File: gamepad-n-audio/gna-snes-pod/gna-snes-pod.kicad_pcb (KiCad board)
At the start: 2 copper layers, 78 x 43 mm, 12 parts, among them J1 SNES, J2 SNES, J3 Gamepads, J4 SNES, J5 SNES

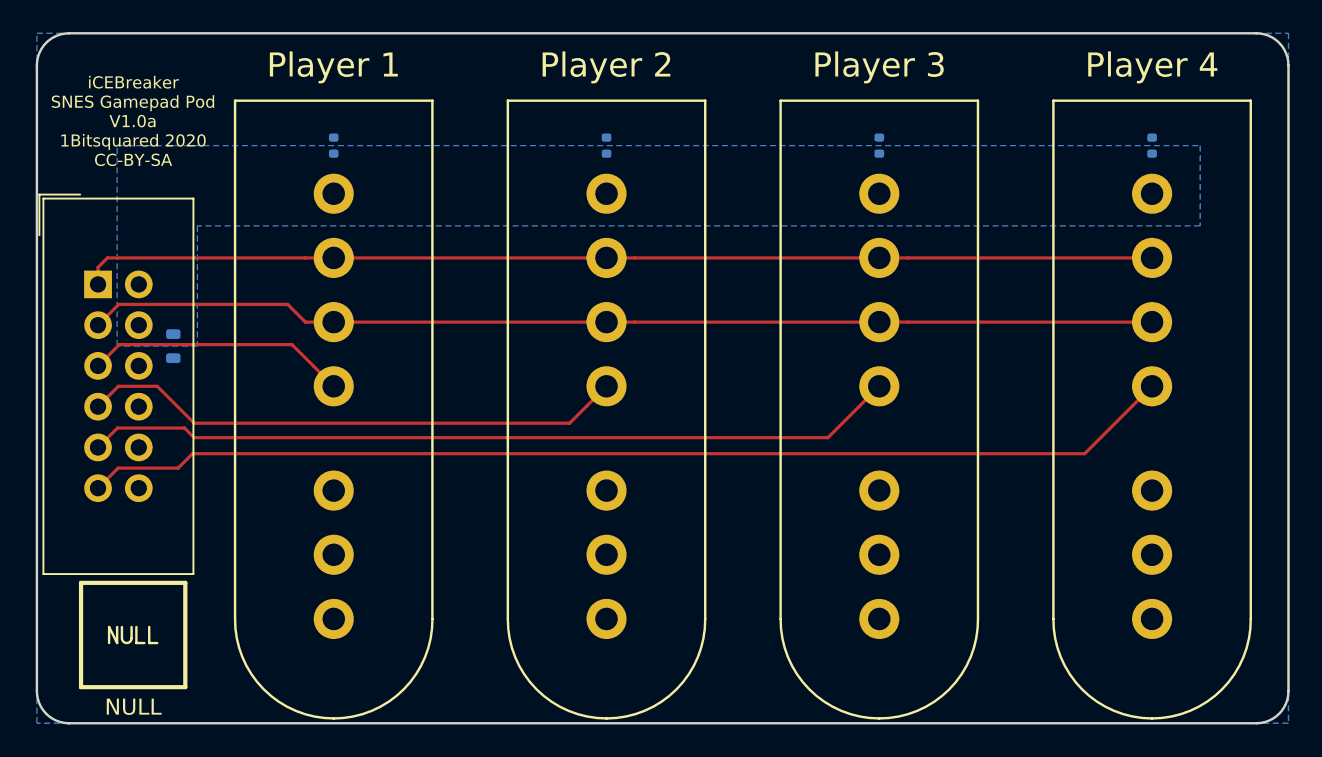
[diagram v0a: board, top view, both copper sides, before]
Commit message: gna SNES pod: Replaced back side ground fill with large traces.
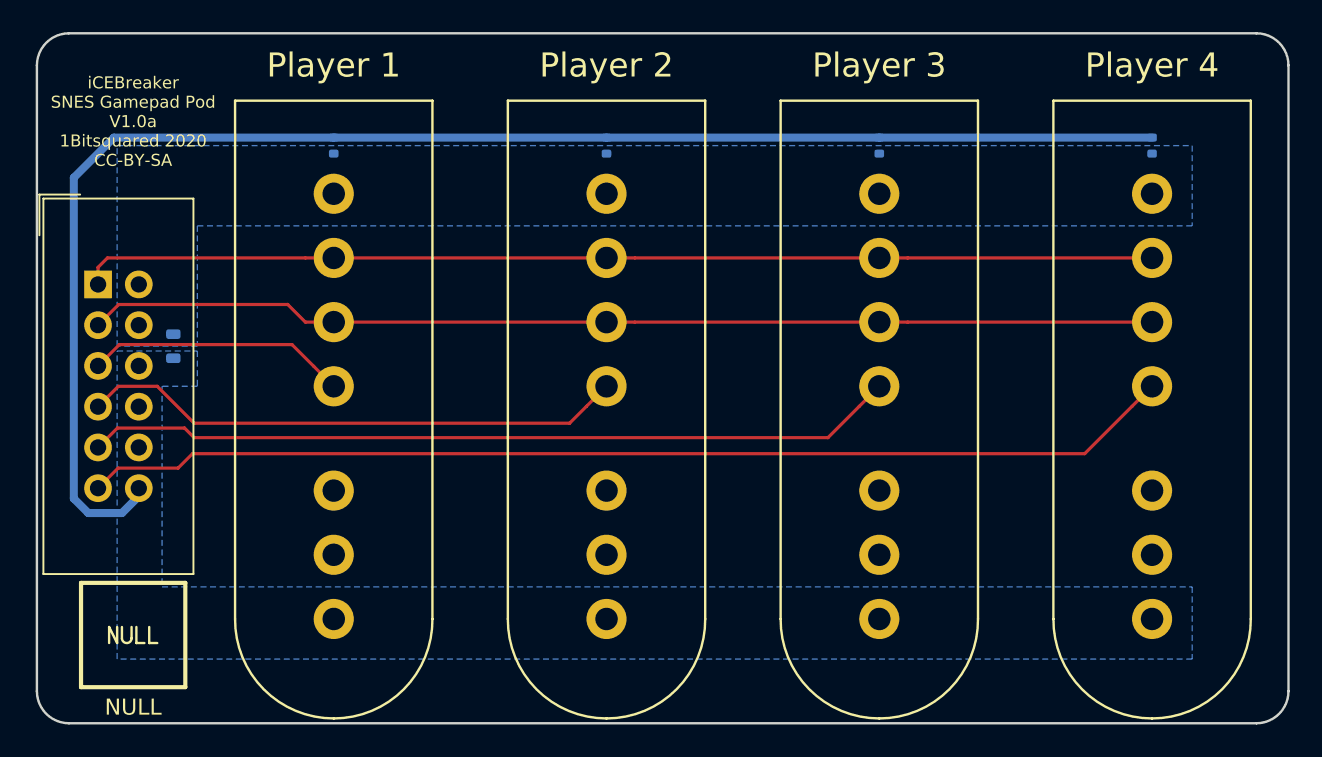
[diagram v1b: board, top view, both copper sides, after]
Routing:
- net GND: track 0.00 -> 93.7 mm

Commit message: gna SL/SNES pod: Bumped version.
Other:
- board text added: "iCEBreaker SNES Gamepad Pod V1.0b 1Bitsquared 2020 CC-BY-SA"
- board text removed: "iCEBreaker SNES Gamepad Pod V1.0a 1Bitsquared 2020 CC-BY-SA"
